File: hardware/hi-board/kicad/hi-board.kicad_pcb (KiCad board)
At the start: 4 copper layers, 54 parts, among them J1 Conn_02x25_Counter_Clockwise, J2 Speaker, SW1 Up, SW2 A, SW3 Down, SW4 B, SW5 Left, SW6 Start, SW7 Right, SW8 Select, U1 LM386, U2 ER-TFT040-2, U3 TLV61046ADB, U4 ME6216A30M3G, U5 LSF0108, U6 LSF0108, U7 LSF0108, U8 LSF0108

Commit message: Add HI board outline
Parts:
- moved C1 225.2 mm to (-85.2, -3.15)
- moved C10 225.2 mm to (-72.9, -12.6)
- moved C11 225.2 mm to (-76.9, -12.6)
- moved C15 225.2 mm to (-76.9, -15.1)
- moved C16 225.2 mm to (-72.9, -15.1)
- moved C17 225.2 mm to (-68.9, -15.1)
- moved C2 225.2 mm to (-89.3, 2.03)
- moved C3 225.2 mm to (-78.0, -5.82)
- moved C4 225.2 mm to (-65.2, -3.31)
- moved C5 225.2 mm to (-61.2, -3.31)
- moved C6 225.2 mm to (-65.6, -0.80)
- moved C7 225.2 mm to (-57.2, -5.82)
- moved C8 225.2 mm to (-68.9, -12.6)
- moved C9 225.2 mm to (-59.4, -18.9)
- moved J1 225.2 mm to (-30.3, -32.8)
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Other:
- board outline added: 81 x 117 mm

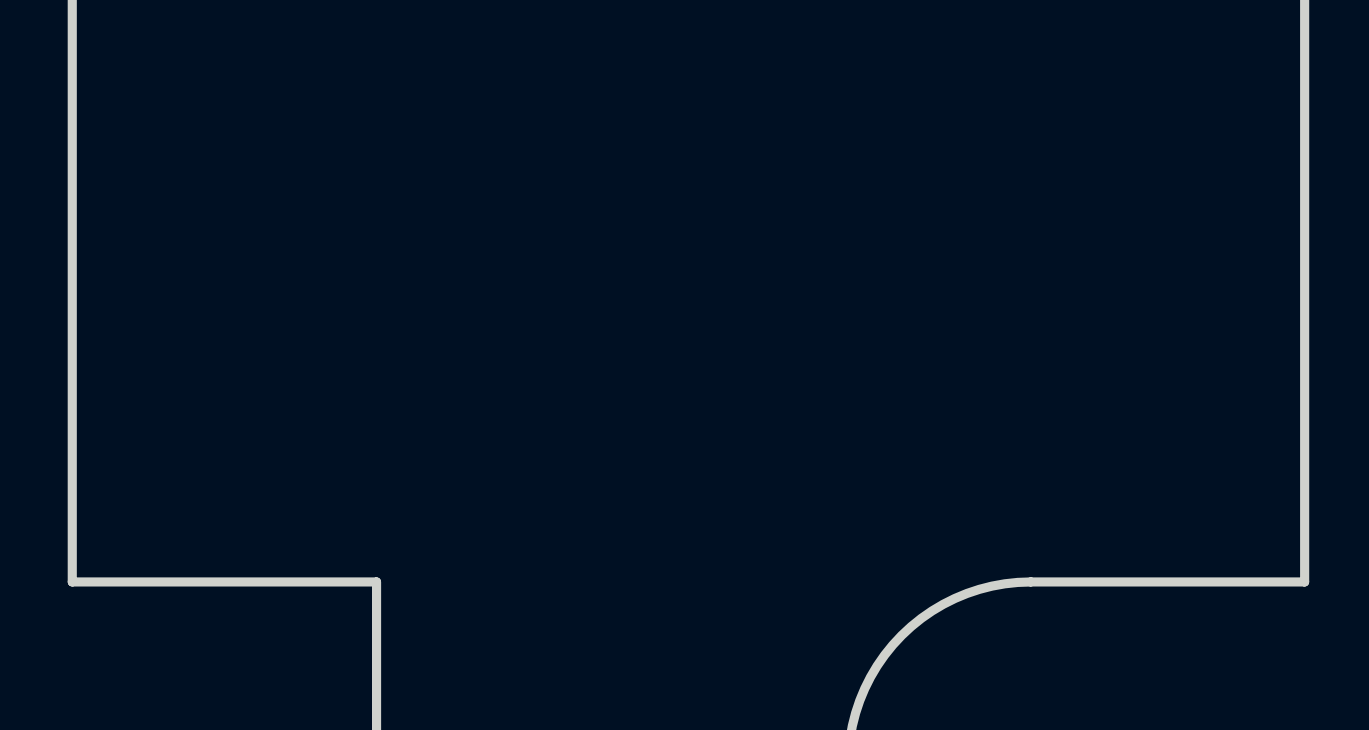
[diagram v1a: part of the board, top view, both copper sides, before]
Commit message: Add mounting holes
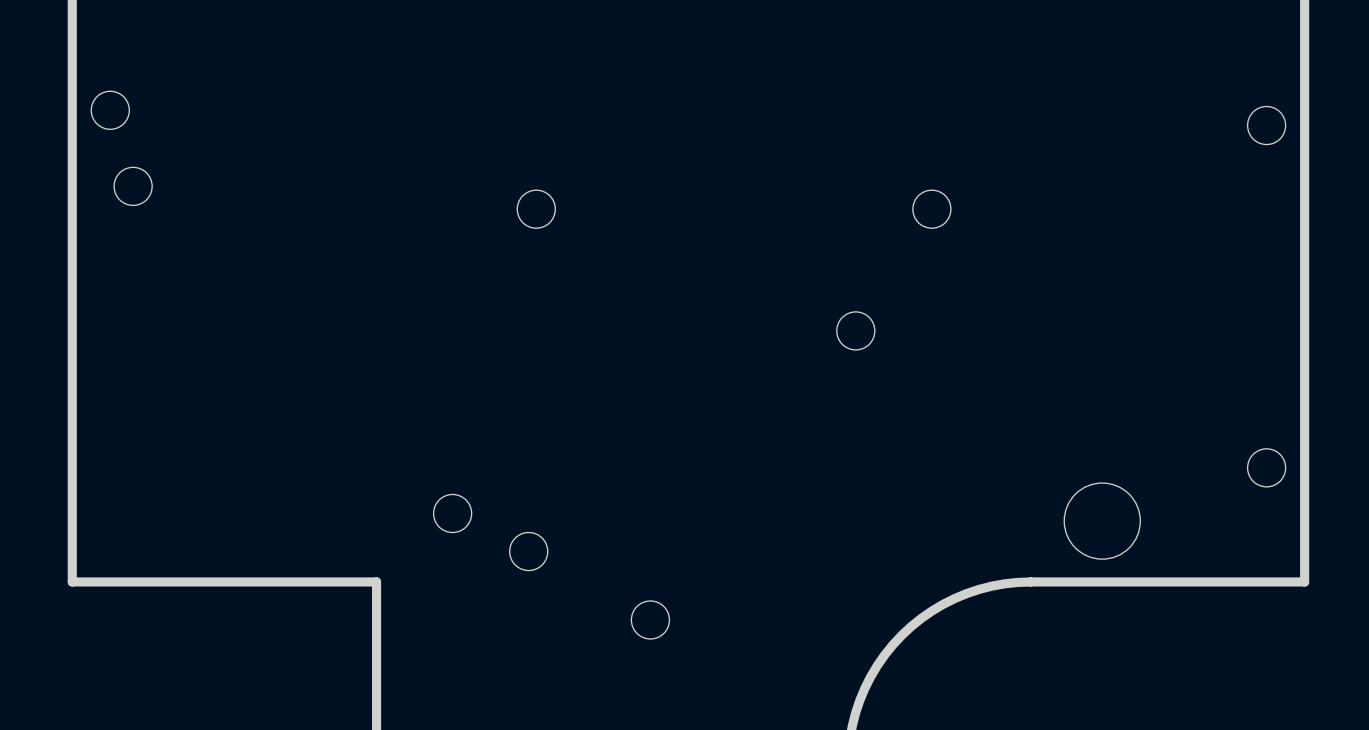
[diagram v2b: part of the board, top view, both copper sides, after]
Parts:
- added REF**: MountingHole_2.5mm, MountingHole:MountingHole_2.5mm, F.Cu at (38.0, -9.50)
- added REF**: MountingHole_2.5mm, MountingHole:MountingHole_2.5mm, F.Cu at (81.0, -27.8)
- added REF**: MountingHole_5mm, MountingHole:MountingHole_5mm, F.Cu at (67.7, -16.0)
- added REF**: MountingHole_2.5mm, MountingHole:MountingHole_2.5mm, F.Cu at (78.5, -19.5)
- added REF**: MountingHole_2.5mm, MountingHole:MountingHole_2.5mm, F.Cu at (30.0, -14.0)
- added REF**: MountingHole_2.5mm, MountingHole:MountingHole_2.5mm, F.Cu at (25.0, -16.5)
- added REF**: MountingHole_2.5mm, MountingHole:MountingHole_2.5mm, F.Cu at (4.00, -38.0)
- added REF**: MountingHole_2.5mm, MountingHole:MountingHole_2.5mm, F.Cu at (2.50, -43.0)
- added REF**: MountingHole_2.5mm, MountingHole:MountingHole_2.5mm, F.Cu at (30.5, -36.5)
- added REF**: MountingHole_2.5mm, MountingHole:MountingHole_2.5mm, F.Cu at (51.5, -28.5)
- added REF**: MountingHole_2.5mm, MountingHole:MountingHole_2.5mm, F.Cu at (56.5, -36.5)
- added REF**: MountingHole_2.5mm, MountingHole:MountingHole_2.5mm, F.Cu at (78.5, -42.0)

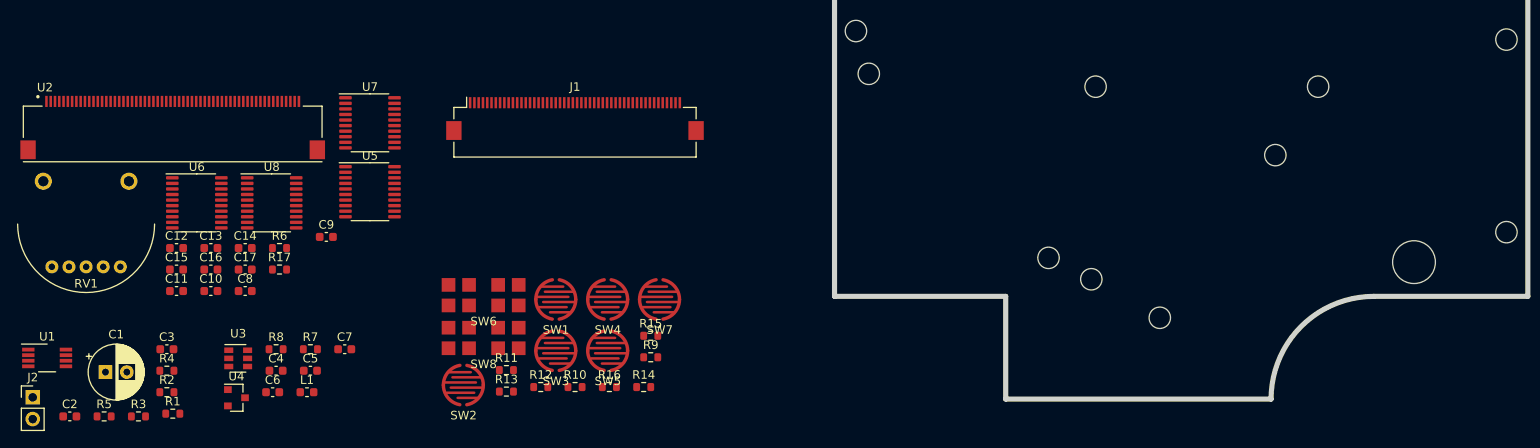
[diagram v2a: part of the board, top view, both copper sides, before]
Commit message: Add joypad footprints to layout
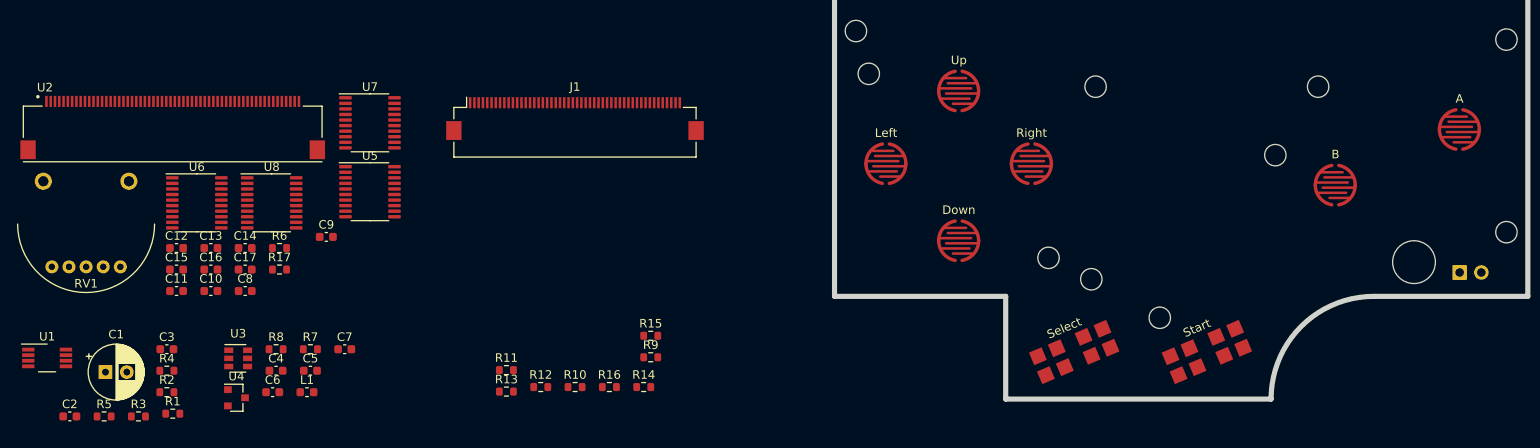
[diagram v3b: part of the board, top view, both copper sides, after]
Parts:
- J2: moved to B.Cu
- moved J2 167.3 mm to (73.0, -14.8), turned to 270 degrees
- moved SW2 120.1 mm to (73.0, -31.5)
- moved SW4 86.1 mm to (58.5, -25.0)
- moved SW6 84.8 mm to (43.5, -5.50), turned to 23 degrees
- moved SW8 69.0 mm to (28.0, -5.50), turned to 23 degrees
- moved SW1 53.0 mm to (14.5, -36.0)
- moved SW3 48.8 mm to (14.5, -18.5)
- moved SW7 46.3 mm to (23.0, -27.5)
- moved SW5 39.2 mm to (6.00, -27.5)

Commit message: Flip mounting holes to bottom side
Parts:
- REF** (x12): moved to B.Cu

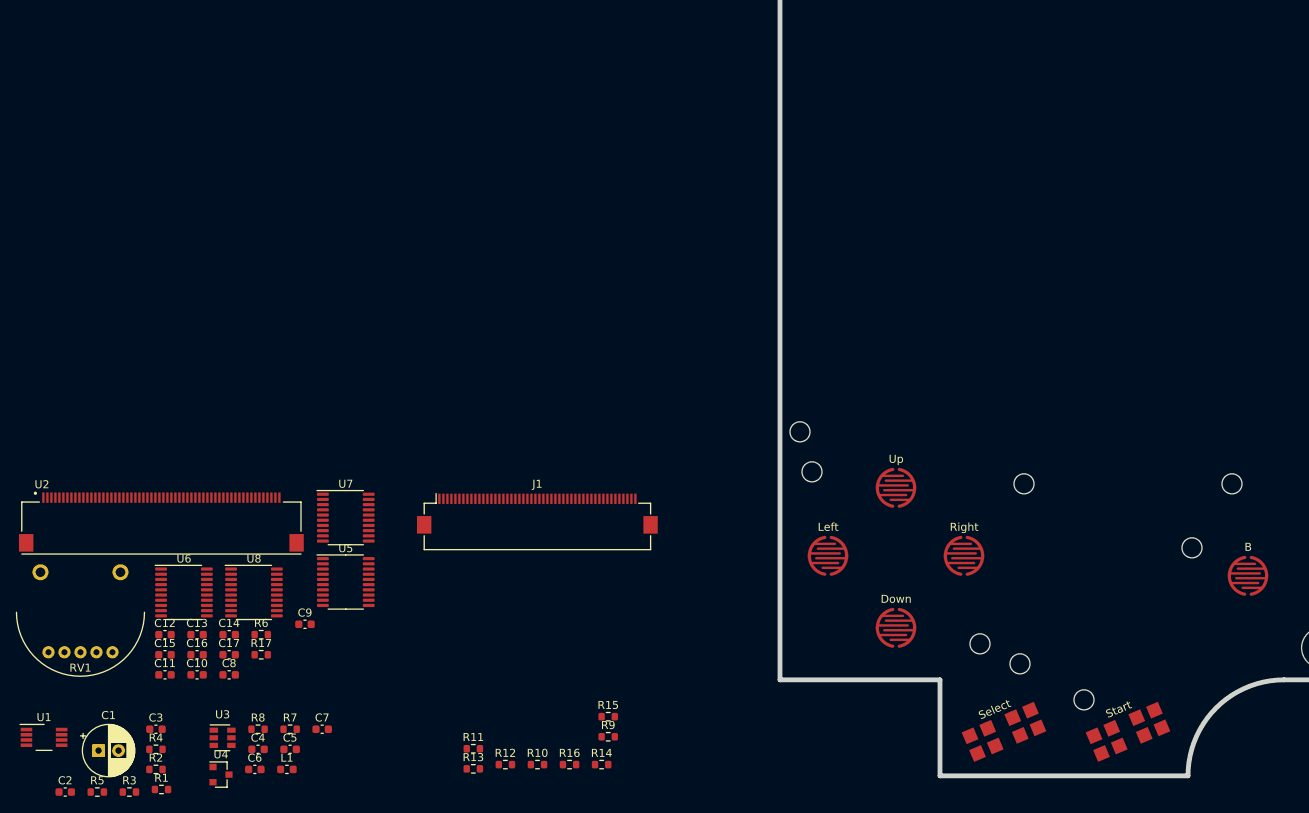
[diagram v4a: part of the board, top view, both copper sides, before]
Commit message: Place connector components
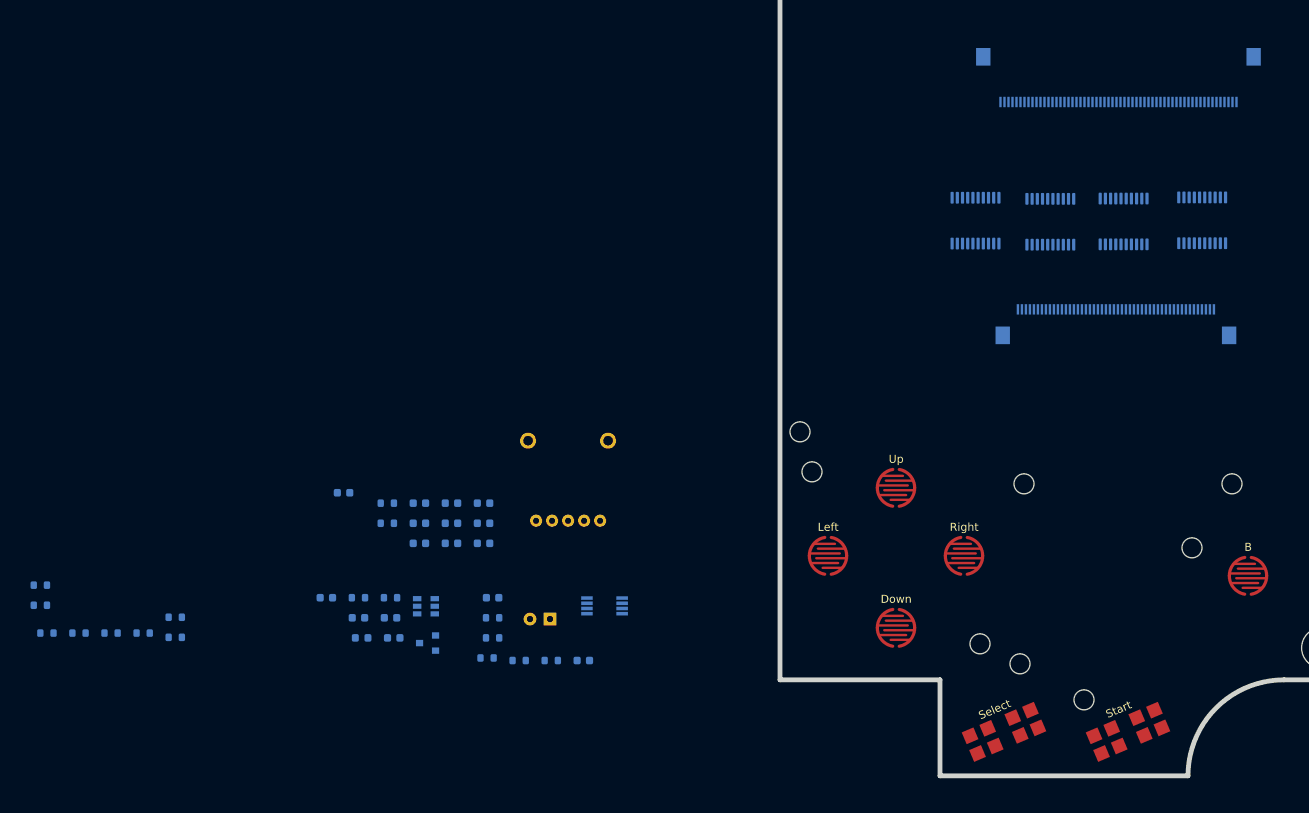
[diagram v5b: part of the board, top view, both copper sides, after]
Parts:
- C1, C10, C11, C12, C13, C14, C15, C16, C17, C2, C3, C4, C5, C6, C7, C8, C9, J1, L1, R1, R10, R11, R12, R13, R14, R15, R16, R17, R2, R3, R4, R5, R6, R7, R8, R9, RV1, U1, U2, U3, U4, U5, U6, U7, U8: moved to B.Cu
- moved U2 129.5 mm to (42.3, -84.2)
- moved U6 126.3 mm to (43.0, -69.3), turned to 90 degrees
- moved U5 116.2 mm to (52.8, -69.4), turned to 90 degrees
- moved U8 101.5 mm to (24.4, -69.4), turned to 90 degrees
- moved U7 95.5 mm to (33.8, -69.3), turned to 90 degrees
- moved J1 76.1 mm to (42.0, -56.5), turned to 180 degrees
- moved R15 72.9 mm to (-92.5, -23.8), turned to 180 degrees
- moved R9 72.9 mm to (-92.5, -21.3), turned to 180 degrees
- moved U1 72.0 mm to (-21.9, -21.2), turned to 180 degrees
- moved R14 71.3 mm to (-91.6, -17.8), turned to 180 degrees
- moved C2 66.8 mm to (-24.6, -14.4), turned to 180 degrees
- moved R16 63.5 mm to (-87.6, -17.8), turned to 180 degrees
- moved RV1 63.1 mm to (-26.5, -36.9), turned to 180 degrees
- moved R5 59.1 mm to (-28.6, -14.4), turned to 180 degrees
- moved C1 58.8 mm to (-28.8, -19.6), turned to 180 degrees
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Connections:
- J1 pad 26: DISP_R4 -> DISP_B0
- J1 pad 27: DISP_R3 -> DISP_B1
- J1 pad 28: DISP_R2 -> DISP_B2
- J1 pad 29: DISP_R1 -> DISP_B3
- J1 pad 30: DISP_R0 -> DISP_B4
- J1 pad 31: DISP_G5 -> DISP_G0
- J1 pad 32: DISP_G4 -> DISP_G1
- J1 pad 33: DISP_G3 -> DISP_G2
- J1 pad 34: DISP_G2 -> DISP_G3
- J1 pad 35: DISP_G1 -> DISP_G4
- J1 pad 36: DISP_G0 -> DISP_G5
- J1 pad 37: DISP_B4 -> DISP_R0
- J1 pad 38: DISP_B3 -> DISP_R1
- J1 pad 39: DISP_B2 -> DISP_R2
- J1 pad 40: DISP_B1 -> DISP_R3
- J1 pad 41: DISP_B0 -> DISP_R4
- U6 pad 10: DISP_G3 -> DISP_G2
- U6 pad 3: DISP_B4 -> DISP_B0
- U6 pad 4: DISP_B3 -> DISP_B1
- U6 pad 6: DISP_B1 -> DISP_B3
- U6 pad 7: DISP_B0 -> DISP_B4
- U6 pad 8: DISP_G5 -> DISP_G0
- U6 pad 9: DISP_G4 -> DISP_G1
- U7 pad 10: DISP_R0 -> DISP_R4
- U7 pad 3: DISP_G2 -> DISP_G3
- U7 pad 4: DISP_G1 -> DISP_G4
- U7 pad 5: DISP_G0 -> DISP_G5
- U7 pad 6: DISP_R4 -> DISP_R0
- U7 pad 7: DISP_R3 -> DISP_R1
- U7 pad 9: DISP_R1 -> DISP_R3

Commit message: Update audio circuit to SMD only
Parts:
- added C18: 100µF (16V), Capacitor_SMD:C_1210_3225Metric, B.Cu at (66.6, -26.7)
- added C19: 100µF (16V), Capacitor_SMD:C_1210_3225Metric, B.Cu at (72.3, -22.5)
- C1: value 220µF -> 100µF (16V); footprint Capacitor_THT:CP_Radial_D6.3mm_P2.50mm -> Capacitor_SMD:C_1210_3225Metric
- moved R1 109.6 mm to (68.3, -46.4)
- moved R3 106.7 mm to (71.0, -39.7)
- moved R2 104.5 mm to (64.4, -46.4)
- moved R4 103.9 mm to (65.6, -41.6)
- moved C2 100.9 mm to (71.9, -44.0)
- moved C3 99.7 mm to (63.3, -31.6)
- moved R5 97.6 mm to (67.5, -31.3)
- moved C1 95.4 mm to (66.6, -22.5), turned to 0 degrees
- moved U1 89.3 mm to (66.2, -35.9)
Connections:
- C3 pad 1: Net-(C1-Pad1) -> Net-(C1-Pad2)
- J2 pad 1: Net-(C1-Pad2) -> Net-(C1-Pad1)
- U1 pad 5: Net-(C1-Pad1) -> Net-(C1-Pad2)
